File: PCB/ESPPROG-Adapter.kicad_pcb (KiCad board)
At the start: 2 copper layers, 37.8 x 25.1 mm, 8 parts, among them J1 Conn_02x05_Odd_Even, J2 CONN ESP-PROG, J3 DebugHeader_Cortex-M_JTAG_10p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, J4 ProgConn-SOICBite, J5 DebugHeader_Cortex-M_SWD_UART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, J6 SOICbite-JTAG

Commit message: nothing major, just a complete redesign for v1.3
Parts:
- removed J4: ProgConn-SOICBite, Connector_IDC:IDC-Header_2x04_P2.54mm_Vertical
- removed J6: SOICbite-JTAG, Connector_IDC:IDC-Header_2x04_P2.54mm_Vertical
- removed JP1: CH_PD EN, Jumper:SolderJumper-2_P1.3mm_Bridged_RoundedPad1.0x1.5mm
- added J7: SOICBite IDC UART, Connector_IDC:IDC-Header_2x04_P2.54mm_Vertical, F.Cu at (147.0, 64.9)
- added J9: SOICBite IDC JTAG, Connector_IDC:IDC-Header_2x04_P2.54mm_Vertical, F.Cu at (121.5, 70.4)
- added JP3: ESPPROG_RX_JUMP, Connector_PinHeader_2.54mm:PinHeader_1x03_P2.54mm_Vertical, F.Cu at (140.5, 69.6)
- added JP4: ESPPROG_TX_JUMP, Connector_PinHeader_2.54mm:PinHeader_1x03_P2.54mm_Vertical, F.Cu at (140.6, 72.0)
- added JP5: TX->RX, Jumper:SolderJumper-2_P1.3mm_Bridged_RoundedPad1.0x1.5mm, B.Cu at (144.2, 77.2)
- added JP6: RX->TX, Jumper:SolderJumper-2_P1.3mm_Bridged_RoundedPad1.0x1.5mm, B.Cu at (148.0, 77.2)
- J5: value DebugHeader_Cortex-M_SWD_UART_10p_TagConnect -> SOICBite connector UART Loopback; footprint jmux-footprints:TC-2050-IDC-SOCKET -> jmux-footprints:SOIC_clipProgSmall
- JP2: value SolderJumper_2_Bridged -> CH_PD EN
- moved J5 20.5 mm to (147.7, 83.5), turned to 0 degrees
- moved JP2 3.76 mm to (147.9, 61.8)
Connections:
- J2 pad 3: /ESP_TXD0 -> /ESPPROG_TX
- J2 pad 5: /ESP_RXD0 -> /ESPPROG_RX
- J5 pad 1: /VDD_U -> unconnected-(J5-VCC-Pad1)
- J5 pad 3: Earth -> unconnected-(J5-GPIO2-Pad3)
- J5 pad 5: Earth -> Net-(J5-RX)
- J5 pad 6: /SWO_IO0 -> Net-(J5-RX)
- J5 pad 7: /ESP_RXD0 -> unconnected-(J5-CH_PD-Pad7)
- J5 pad 8: /ESP_TXD0 -> unconnected-(J5-RST-Pad8)
- JP2 pad 1: /SWO_IO0 -> /CH_PD
- JP2 pad 2: /ESP_BOOT -> /VDD_U
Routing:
- net /VDD_U: track 103.9 -> 68.7 mm
- net /ESP_TXD0: track 21.3 -> 40.1 mm, vias 2 -> 0
- net /ESPPROG_RX: track 0.00 -> 18.3 mm
- net /SWO_IO0: track 17.9 -> 0.00 mm, vias 3 -> 0
- net /ESPPROG_TX: track 0.00 -> 17.3 mm
- net /ESP_BOOT: track 19.6 -> 8.55 mm, vias 1 -> 0
- net Earth: track 10.2 -> 0.00 mm, vias 9 -> 8
- net /ESP_RXD0: track 27.4 -> 19.2 mm, vias 1 -> 0
- net /ESP_TMS: track 18.3 -> 25.7 mm
- net /ESP_TCK: track 38.6 -> 31.7 mm
- net /ESP_EN: track 34.0 -> 29.8 mm, vias 2 -> 1
- net /CH_PD: track 4.13 -> 7.54 mm, vias 1 -> 0
- net /ESP_TDI: track 40.3 -> 38.7 mm, vias 2 -> 0
- net /ESP_TDO: track 29.0 -> 27.7 mm, vias 4 -> 2
- net Net-(J5-RX): track 0.00 -> 1.27 mm
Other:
- board text added: "0xjmux v1.3 01-2024"
- board text added: "ESP-PROG Universal Adapter"
- board text added: "JLCJLCJLCJLC"
- board text added: "RX←"
- board text added: "RX←TX"
- board text added: "RX→TX"
- board text added: "Remember to cut solderbridges first!"
- board text added: "SOICBite UART Loopback"
- board text added: "→TX"
- board text removed: "0xjmux v1.2 11-2023"
- board text removed: "CH_PD EN"
- board text removed: "ESP-PROG Cable Adapter"
- board text removed: "TC-2050 UART"
- board text removed: "x"

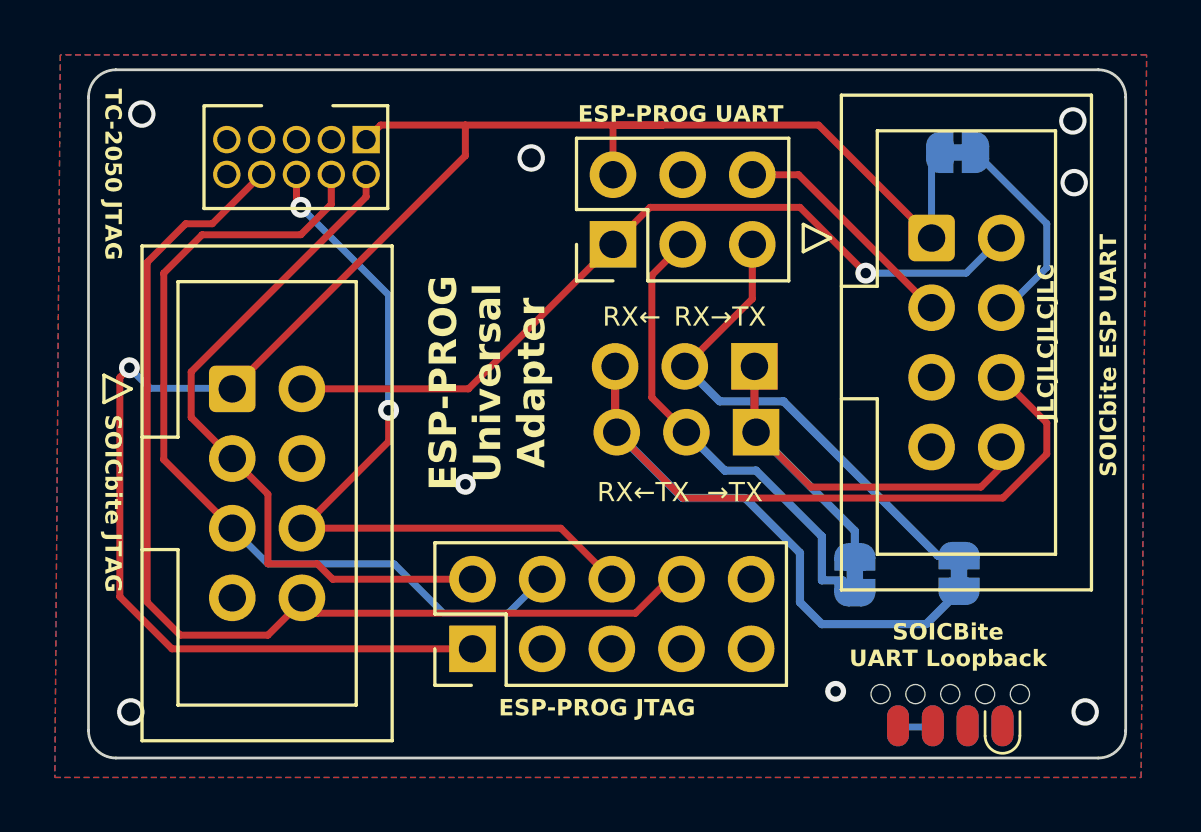
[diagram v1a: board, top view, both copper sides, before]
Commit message: Writeup and minor changes for v1.4
v1.3 arrived and all functionality was confirmed working. This commit
adds the writeup, license, and some small modifications to the PCB to
make it a little easier to use.

* PCB updated to clarify assembly and use (text enlarged, dual 1x3 headers for reversible UART changed to single 2x3P using custom symbol).
* Vdd for JTAG and UART disconnected from each other on adapter, allowing different voltage to be used for each.
* Connected nRST line of ESP-PROG (from UART header) to board RESET line on JTAG pinout with solderjumper.
* Default connected solderjumpers changed to default open for Reversible UART, since I anticipate it'll be more used than not.
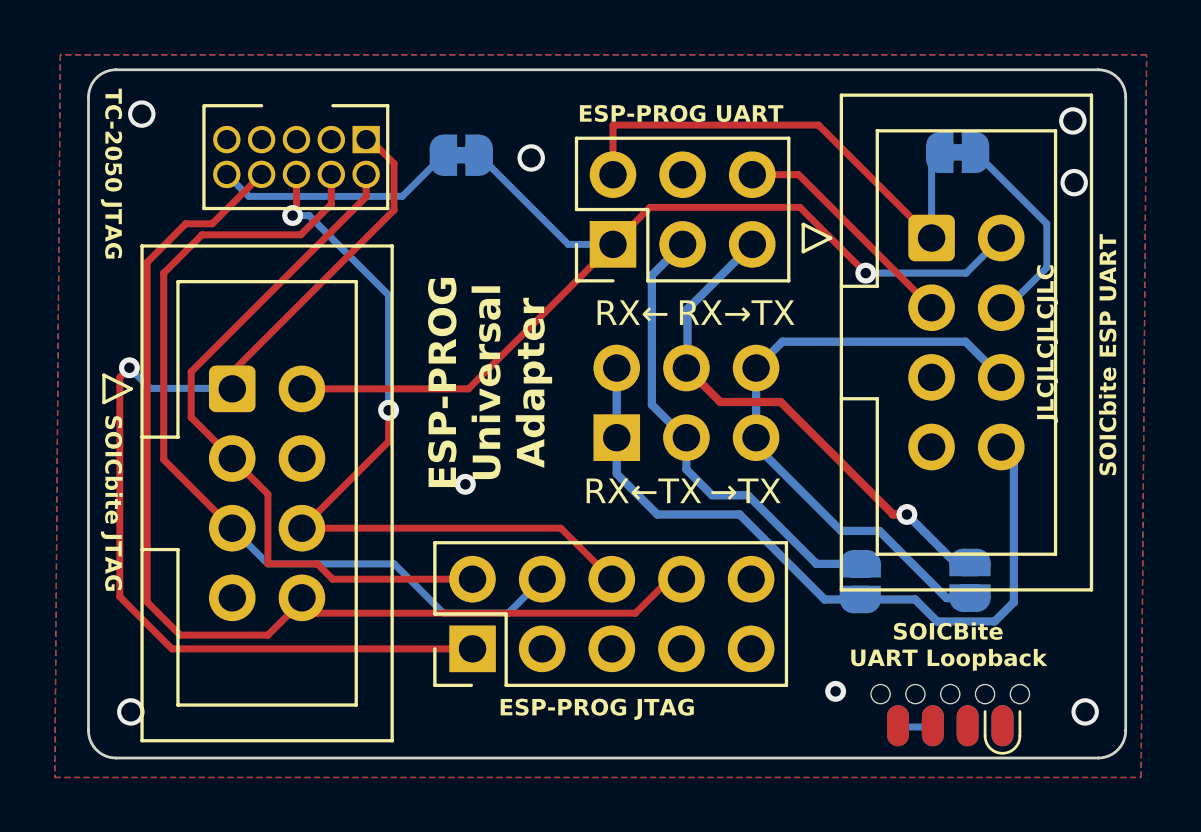
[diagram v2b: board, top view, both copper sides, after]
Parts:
- removed JP3: ESPPROG_RX_JUMP, Connector_PinHeader_2.54mm:PinHeader_1x03_P2.54mm_Vertical
- removed JP4: ESPPROG_TX_JUMP, Connector_PinHeader_2.54mm:PinHeader_1x03_P2.54mm_Vertical
- added JP1: ESPPROG_TX_RX_JUMP, Connector_PinHeader_2.54mm:PinHeader_2x03_P2.54mm_Vertical, F.Cu at (135.5, 72.2)
- added JP7: JTAG ~{RST}, Jumper:SolderJumper-2_P1.3mm_Bridged_RoundedPad1.0x1.5mm, B.Cu at (129.8, 61.9)
- JP5: value TX->RX -> TX→RX; footprint Jumper:SolderJumper-2_P1.3mm_Bridged_RoundedPad1.0x1.5mm -> Jumper:SolderJumper-2_P1.3mm_Open_RoundedPad1.0x1.5mm
- JP6: value RX->TX -> RX→TX; footprint Jumper:SolderJumper-2_P1.3mm_Bridged_RoundedPad1.0x1.5mm -> Jumper:SolderJumper-2_P1.3mm_Open_RoundedPad1.0x1.5mm
- moved JP6 0.47 mm to (148.4, 77.4)
- moved JP5 0.32 mm to (144.4, 77.5)
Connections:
- J1 pad 1: /VDD_U -> /JTAG_VDD
- J3 pad 1: /VDD_U -> /JTAG_VDD
- J3 pad 10: unconnected-(J3-~{RESET}-Pad10) -> Net-(J3-~{RESET})
- J9 pad 1: /VDD_U -> /JTAG_VDD
- JP5 pad 1: /ESPPROG_TX -> /ESP_RXD0
- JP5 pad 2: /ESP_RXD0 -> /ESPPROG_TX
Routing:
- net /VDD_U: track 68.7 -> 18.0 mm, vias 1 -> 0
- net /JTAG_VDD: track 0.00 -> 37.5 mm, vias 0 -> 1
- net /ESP_TXD0: track 40.1 -> 22.5 mm
- net Net-(J3-~{RESET}): track 0.00 -> 8.85 mm
- net /ESP_RXD0: track 19.2 -> 26.1 mm
- net /ESP_EN: track 29.8 -> 36.0 mm
- net /ESPPROG_RX: track 18.3 -> 18.2 mm, vias 0 -> 1
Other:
- board text added: "0xjmux v1.4 02-2024"
- board text removed: "0xjmux v1.3 01-2024"
- board text removed: "Remember to cut solderbridges first!"
